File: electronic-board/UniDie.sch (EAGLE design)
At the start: 23 parts, among them IC1 ATMEGA88-THIN, J2 AVR_SPI_PROG_3X2NS

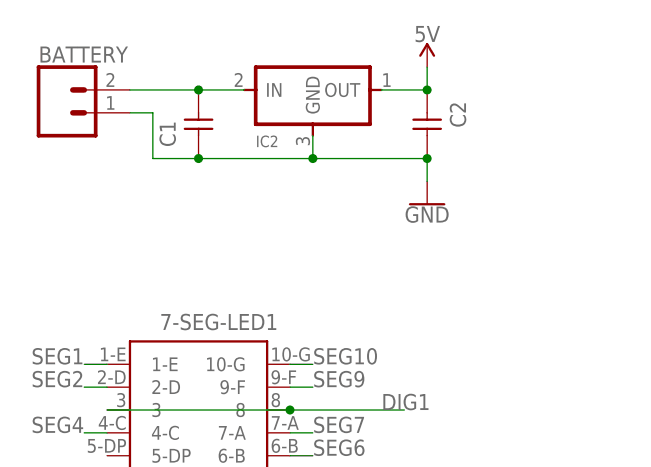
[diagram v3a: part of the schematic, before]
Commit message: Added circuit breaker to board to switch on/off power
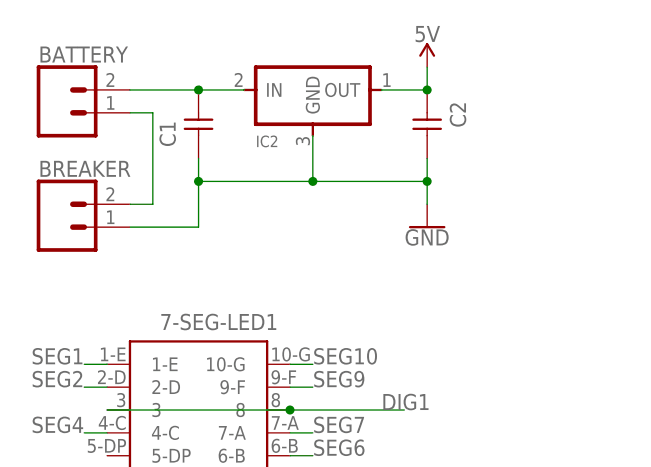
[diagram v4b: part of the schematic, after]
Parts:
- added BREAKER: (no value), SparkFun-Connectors:CONN_021X02_NO_SILK
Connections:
- new net N$5: BATTERY.1, BREAKER.2
- net GND: now also BREAKER.1; no longer BATTERY.1
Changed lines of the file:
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@@
 <part name="J3" library="SparkFun-Connectors" deviceset="CONN_01" device="PTH_NO_SILK_YES_STOP"/>
 <part name="BATTERY" library="SparkFun-Connectors" deviceset="CONN_02" device="1X02_NO_SILK"/>
+<part name="BREAKER" library="SparkFun-Connectors" deviceset="CONN_02" device="1X02_NO_SILK"/>
 </parts>
 <sheets>
@@
 <instance part="GND1" gate="1" x="238.76" y="60.96"/>
 <instance part="GND2" gate="1" x="220.98" y="38.1"/>
-<instance part="GND3" gate="1" x="68.58" y="58.42"/>
+<instance part="GND3" gate="1" x="68.58" y="55.88"/>
 <instance part="GND4" gate="1" x="96.52" y="50.8"/>
 <instance part="7-SEG-LED1" gate="G$1" x="43.18" y="35.56" rot="R270"/>
@@
 <instance part="J3" gate="G$1" x="218.44" y="17.78" rot="R90"/>
 <instance part="BATTERY" gate="G$1" x="27.94" y="68.58"/>
+<instance part="BREAKER" gate="G$1" x="27.94" y="55.88"/>
 </instances>
 <busses>
@@
 <net name="GND" class="0">
 <segment>
-<pinref part="C1" gate="&gt;NAME" pin="1"/>
-<wire x1="43.18" y1="63.5" x2="38.1" y2="63.5" width="0.1524" layer="91"/>
-<wire x1="38.1" y1="63.5" x2="38.1" y2="68.58" width="0.1524" layer="91"/>
-<wire x1="38.1" y1="68.58" x2="35.56" y2="68.58" width="0.1524" layer="91"/>
-<pinref part="IC2" gate="G$1" pin="GND"/>
-<wire x1="55.88" y1="66.04" x2="55.88" y2="63.5" width="0.1524" layer="91"/>
-<wire x1="55.88" y1="63.5" x2="43.18" y2="63.5" width="0.1524" layer="91"/>
-<junction x="43.18" y="63.5"/>
 <pinref part="C2" gate="&gt;NAME" pin="2"/>
-<wire x1="55.88" y1="63.5" x2="68.58" y2="63.5" width="0.1524" layer="91"/>
-<junction x="55.88" y="63.5"/>
 <pinref part="GND3" gate="1" pin="GND"/>
 <wire x1="68.58" y1="63.5" x2="68.58" y2="60.96" width="0.1524" layer="91"/>
-<junction x="68.58" y="63.5"/>
-<pinref part="BATTERY" gate="G$1" pin="1"/>
+<pinref part="IC2" gate="G$1" pin="GND"/>
+<wire x1="68.58" y1="60.96" x2="68.58" y2="58.42" width="0.1524" layer="91"/>
+<wire x1="55.88" y1="66.04" x2="55.88" y2="60.96" width="0.1524" layer="91"/>
+<pinref part="BREAKER" gate="G$1" pin="1"/>
+<pinref part="C1" gate="&gt;NAME" pin="1"/>
+<wire x1="43.18" y1="63.5" x2="43.18" y2="60.96" width="0.1524" layer="91"/>
+<wire x1="43.18" y1="60.96" x2="43.18" y2="55.88" width="0.1524" layer="91"/>
+<wire x1="43.18" y1="55.88" x2="35.56" y2="55.88" width="0.1524" layer="91"/>
+<wire x1="55.88" y1="60.96" x2="43.18" y2="60.96" width="0.1524" layer="91"/>
+<junction x="43.18" y="60.96"/>
+<wire x1="55.88" y1="60.96" x2="68.58" y2="60.96" width="0.1524" layer="91"/>
+<junction x="55.88" y="60.96"/>
+<junction x="68.58" y="60.96"/>
 </segment>
 <segment>
@@
 </segment>
 </net>
+<net name="N$5" class="0">
+<segment>
+<pinref part="BREAKER" gate="G$1" pin="2"/>
+<wire x1="35.56" y1="58.42" x2="38.1" y2="58.42" width="0.1524" layer="91"/>
+<wire x1="38.1" y1="58.42" x2="38.1" y2="68.58" width="0.1524" layer="91"/>
+<pinref part="BATTERY" gate="G$1" pin="1"/>
+<wire x1="38.1" y1="68.58" x2="35.56" y2="68.58" width="0.1524" layer="91"/>
+</segment>
+</net>

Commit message: Adapted parts and routes for milling. Prepared milling files
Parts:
- removed IC2: (no value), fab:REGULATORSOT23
- removed J2: AVR_SPI_PROG_3X2NS, SparkFun-Connectors:AVR_SPI_PROG_3X2NS
- added U$1: 5V-REG, AG:5V-REG
- added U$2: AVRISP, fab:AVRISP
- 7-SEG-LED1, 7-SEG-LED2: value (none) -> LDS-SMHTA304RISITR
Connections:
- net 5V: now also U$1.OUT, U$2.VCC; no longer IC2.OUT, J2.2
- net GND: now also U$1.GND, U$2.GND; no longer IC2.GND, J2.6
- net MISO: now also U$2.MISO; no longer J2.1
- net MOSI: now also U$2.MOSI; no longer J2.4
- net N$1: now also U$1.IN; no longer IC2.IN
- net RST: now also U$2.RST; no longer J2.5
- net SCK: now also U$2.SCK; no longer J2.3

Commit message: Revert "Adapted parts and routes for milling. Prepared milling files"
This reverts commit d229ee454f50b57581f4fd08392e80f763665f52.
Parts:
- removed U$1: 5V-REG, AG:5V-REG
- removed U$2: AVRISP, fab:AVRISP
- added IC2: (no value), fab:REGULATORSOT23
- added J2: AVR_SPI_PROG_3X2NS, SparkFun-Connectors:AVR_SPI_PROG_3X2NS
- 7-SEG-LED1, 7-SEG-LED2: value LDS-SMHTA304RISITR -> (none)
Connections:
- net 5V: now also IC2.OUT, J2.2; no longer U$1.OUT, U$2.VCC
- net GND: now also IC2.GND, J2.6; no longer U$1.GND, U$2.GND
- net MISO: now also J2.1; no longer U$2.MISO
- net MOSI: now also J2.4; no longer U$2.MOSI
- net N$1: now also IC2.IN; no longer U$1.IN
- net RST: now also J2.5; no longer U$2.RST
- net SCK: now also J2.3; no longer U$2.SCK
